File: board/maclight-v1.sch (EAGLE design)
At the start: 52 parts, among them IC1 ATMEGA48/88/168-MU, Y1 20MHz

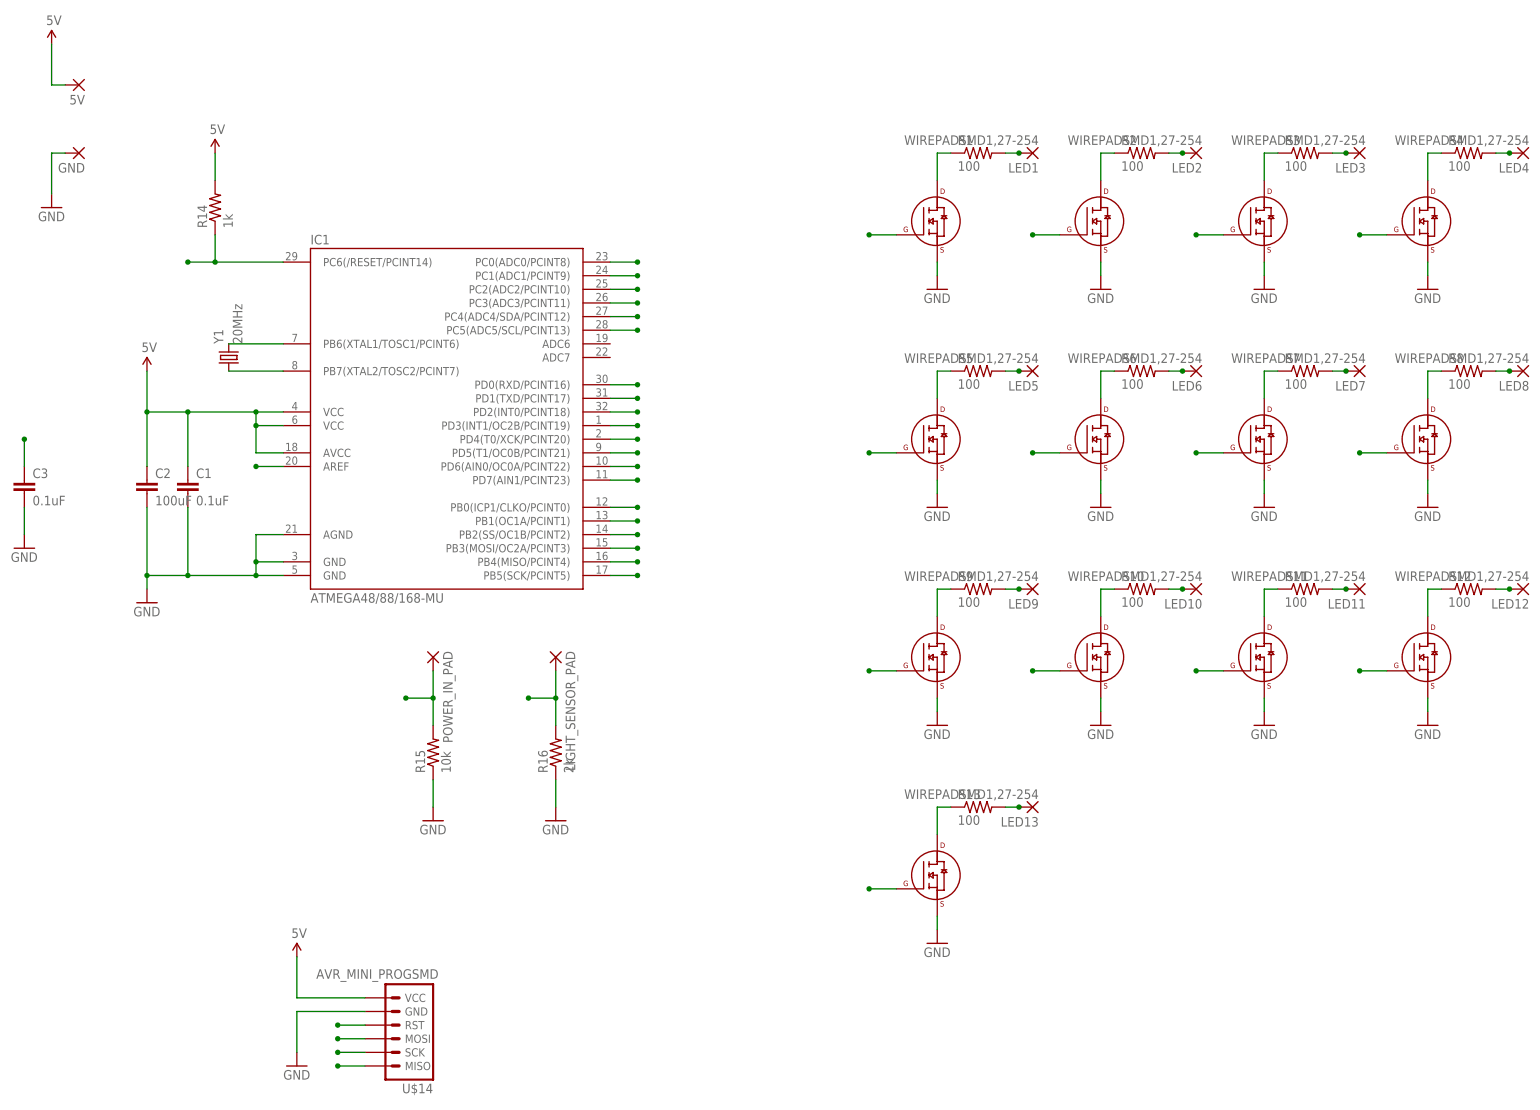
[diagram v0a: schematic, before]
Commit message: Adding new board layout with LED driver (copied from Enterprise project)
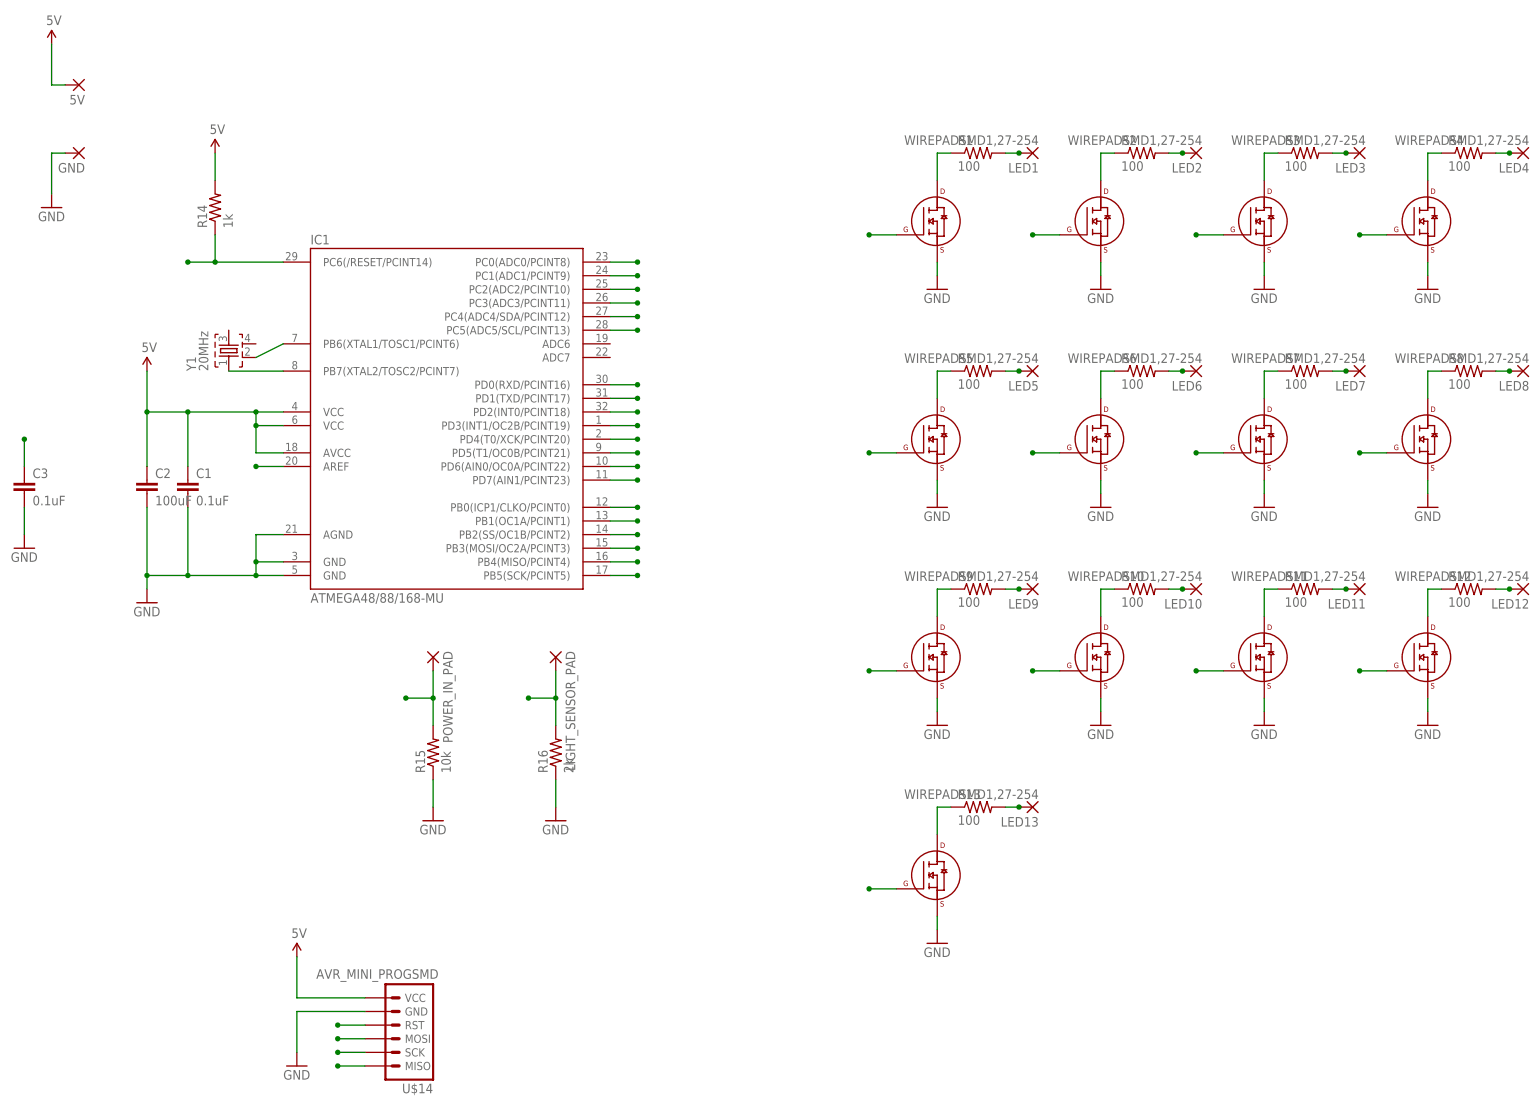
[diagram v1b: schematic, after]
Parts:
- Y1: device SparkFun-FreqCtrl:CRYSTAL5X3 -> crystal:FA-20H
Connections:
- net GND: now also U$1.S, U$10.S, U$11.S, U$12.S, U$13.S, U$2.S, U$3.S, U$4.S, U$5.S, U$6.S, U$7.S, U$8.S, U$9.S
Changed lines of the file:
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@@
 <parts>
 <part name="IC1" library="atmega8" deviceset="ATMEGA48/88/168" device="-MU"/>
-<part name="Y1" library="SparkFun-FreqCtrl" deviceset="CRYSTAL" device="5X3" value="20MHz"/>
+<part name="Y1" library="crystal" deviceset="FA-" device="20H" value="20MHz"/>
 <part name="SUPPLY1" library="SparkFun-Aesthetics" deviceset="5V" device=""/>
 <part name="GND1" library="SparkFun-Aesthetics" deviceset="GND" device=""/>
@@
 <net name="GND" class="0">
 <segment>
-<wire x1="160.02" y1="76.2" x2="160.02" y2="73.66" width="0.1524" layer="91"/>
 <pinref part="GND2" gate="1" pin="GND"/>
-</segment>
-<segment>
-<wire x1="190.5" y1="76.2" x2="190.5" y2="73.66" width="0.1524" layer="91"/>
+<pinref part="U$1" gate="G$1" pin="S"/>
+<wire x1="160.02" y1="76.1746" x2="160.02" y2="73.66" width="0.1524" layer="91"/>
+</segment>
+<segment>
 <pinref part="GND3" gate="1" pin="GND"/>
-</segment>
-<segment>
-<wire x1="220.98" y1="76.2" x2="220.98" y2="73.66" width="0.1524" layer="91"/>
+<pinref part="U$2" gate="G$1" pin="S"/>
+<wire x1="190.5" y1="76.1746" x2="190.5" y2="73.66" width="0.1524" layer="91"/>
+</segment>
+<segment>
 <pinref part="GND4" gate="1" pin="GND"/>
-</segment>
-<segment>
-<wire x1="251.46" y1="76.2" x2="251.46" y2="73.66" width="0.1524" layer="91"/>
+<pinref part="U$3" gate="G$1" pin="S"/>
+<wire x1="220.98" y1="76.1746" x2="220.98" y2="73.66" width="0.1524" layer="91"/>
+</segment>
+<segment>
 <pinref part="GND5" gate="1" pin="GND"/>
-</segment>
-<segment>
-<wire x1="160.02" y1="35.56" x2="160.02" y2="33.02" width="0.1524" layer="91"/>
+<pinref part="U$4" gate="G$1" pin="S"/>
+<wire x1="251.46" y1="76.1746" x2="251.46" y2="73.66" width="0.1524" layer="91"/>
+</segment>
+<segment>
 <pinref part="GND6" gate="1" pin="GND"/>
-</segment>
-<segment>
-<wire x1="190.5" y1="35.56" x2="190.5" y2="33.02" width="0.1524" layer="91"/>
+<pinref part="U$5" gate="G$1" pin="S"/>
+<wire x1="160.02" y1="35.5346" x2="160.02" y2="33.02" width="0.1524" layer="91"/>
+</segment>
+<segment>
 <pinref part="GND7" gate="1" pin="GND"/>
-</segment>
-<segment>
-<wire x1="220.98" y1="35.56" x2="220.98" y2="33.02" width="0.1524" layer="91"/>
+<pinref part="U$6" gate="G$1" pin="S"/>
+<wire x1="190.5" y1="35.5346" x2="190.5" y2="33.02" width="0.1524" layer="91"/>
+</segment>
+<segment>
 <pinref part="GND8" gate="1" pin="GND"/>
-</segment>
-<segment>
-<wire x1="251.46" y1="35.56" x2="251.46" y2="33.02" width="0.1524" layer="91"/>
+<pinref part="U$7" gate="G$1" pin="S"/>
+<wire x1="220.98" y1="35.5346" x2="220.98" y2="33.02" width="0.1524" layer="91"/>
+</segment>
+<segment>
 <pinref part="GND9" gate="1" pin="GND"/>
-</segment>
-<segment>
-<wire x1="160.02" y1="-5.08" x2="160.02" y2="-7.62" width="0.1524" layer="91"/>
+<pinref part="U$8" gate="G$1" pin="S"/>
+<wire x1="251.46" y1="35.5346" x2="251.46" y2="33.02" width="0.1524" layer="91"/>
+</segment>
+<segment>
 <pinref part="GND10" gate="1" pin="GND"/>
-</segment>
-<segment>
-<wire x1="190.5" y1="-5.08" x2="190.5" y2="-7.62" width="0.1524" layer="91"/>
+<pinref part="U$9" gate="G$1" pin="S"/>
+<wire x1="160.02" y1="-5.1054" x2="160.02" y2="-7.62" width="0.1524" layer="91"/>
+</segment>
+<segment>
 <pinref part="GND11" gate="1" pin="GND"/>
-</segment>
-<segment>
-<wire x1="220.98" y1="-5.08" x2="220.98" y2="-7.62" width="0.1524" layer="91"/>
+<pinref part="U$10" gate="G$1" pin="S"/>
+<wire x1="190.5" y1="-5.1054" x2="190.5" y2="-7.62" width="0.1524" layer="91"/>
+</segment>
+<segment>
 <pinref part="GND12" gate="1" pin="GND"/>
-</segment>
-<segment>
-<wire x1="251.46" y1="-5.08" x2="251.46" y2="-7.62" width="0.1524" layer="91"/>
+<pinref part="U$11" gate="G$1" pin="S"/>
+<wire x1="220.98" y1="-5.1054" x2="220.98" y2="-7.62" width="0.1524" layer="91"/>
+</segment>
+<segment>
 <pinref part="GND13" gate="1" pin="GND"/>
-</segment>
-<segment>
-<wire x1="160.02" y1="-45.72" x2="160.02" y2="-48.26" width="0.1524" layer="91"/>
+<pinref part="U$12" gate="G$1" pin="S"/>
+<wire x1="251.46" y1="-5.1054" x2="251.46" y2="-7.62" width="0.1524" layer="91"/>
+</segment>
+<segment>
 <pinref part="GND14" gate="1" pin="GND"/>
+<pinref part="U$13" gate="G$1" pin="S"/>
+<wire x1="160.02" y1="-45.7454" x2="160.02" y2="-48.26" width="0.1524" layer="91"/>
 </segment>
 <segment>
@@
 <pinref part="Y1" gate="G$1" pin="2"/>
 <pinref part="IC1" gate="1" pin="PB6(XTAL1/TOSC1/PCINT6)"/>
-<wire x1="27.94" y1="60.96" x2="38.1" y2="60.96" width="0.1524" layer="91"/>
-</segment>
-</net>
+<wire x1="33.02" y1="58.42" x2="38.1" y2="60.96" width="0.1524" layer="91"/>
+</segment>
+</net>
